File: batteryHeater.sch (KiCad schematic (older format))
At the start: 30 parts

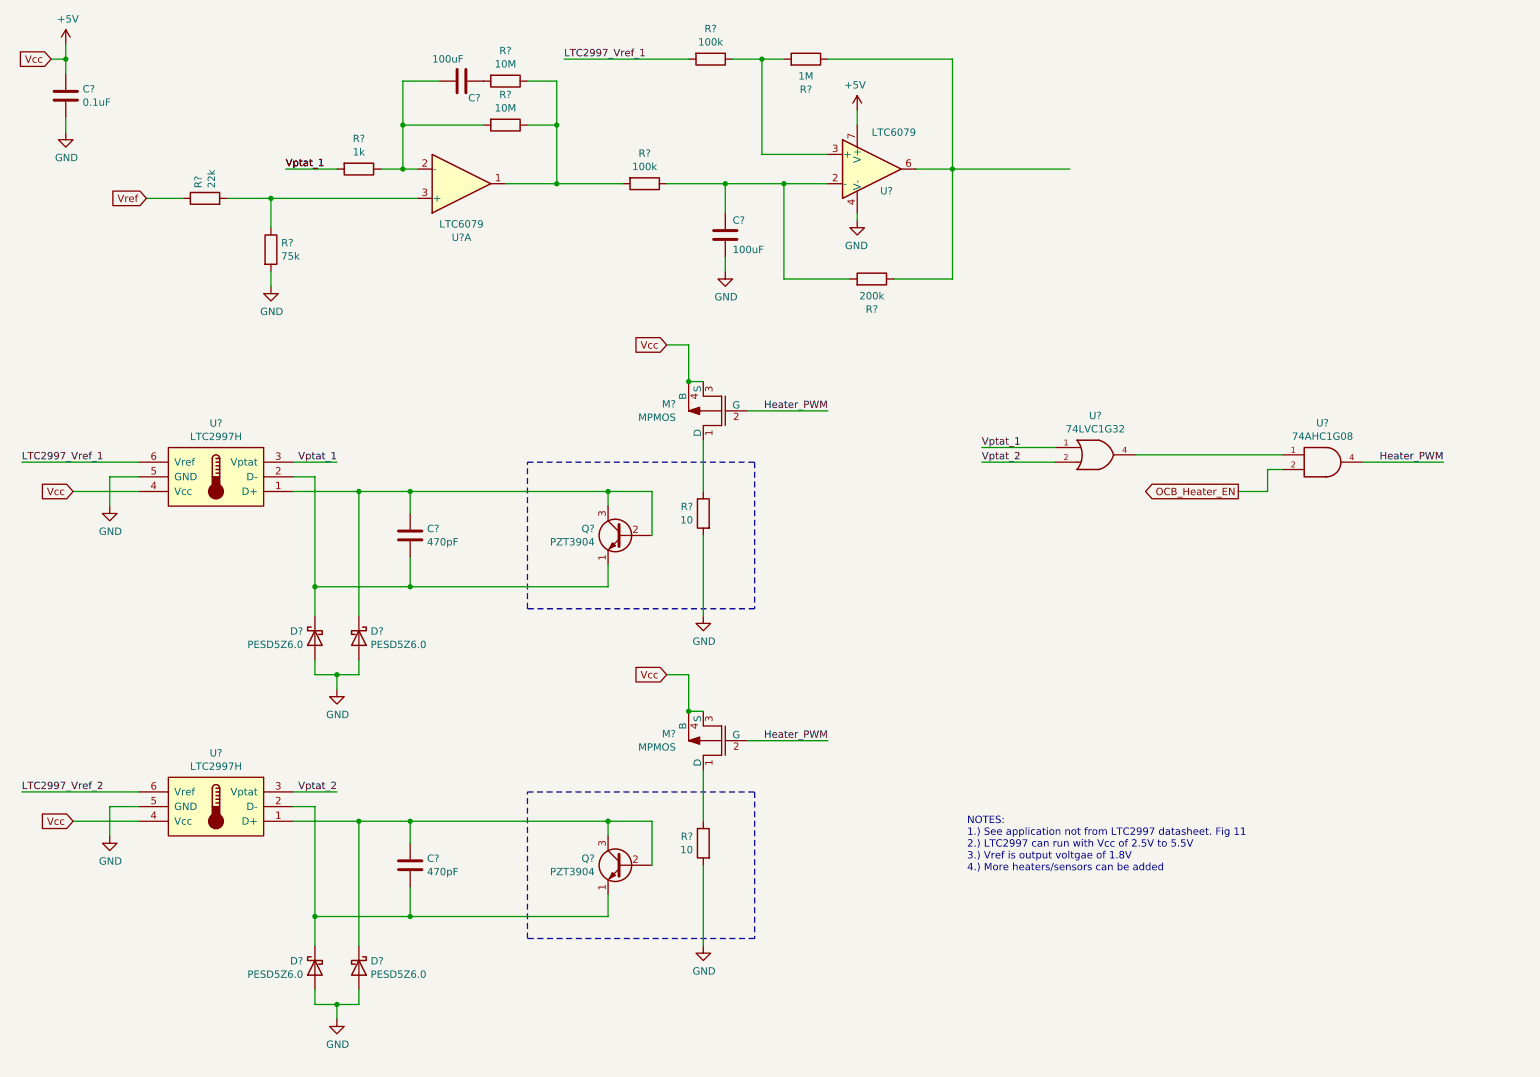
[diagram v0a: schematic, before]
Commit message: added notes for battery heater circuit.
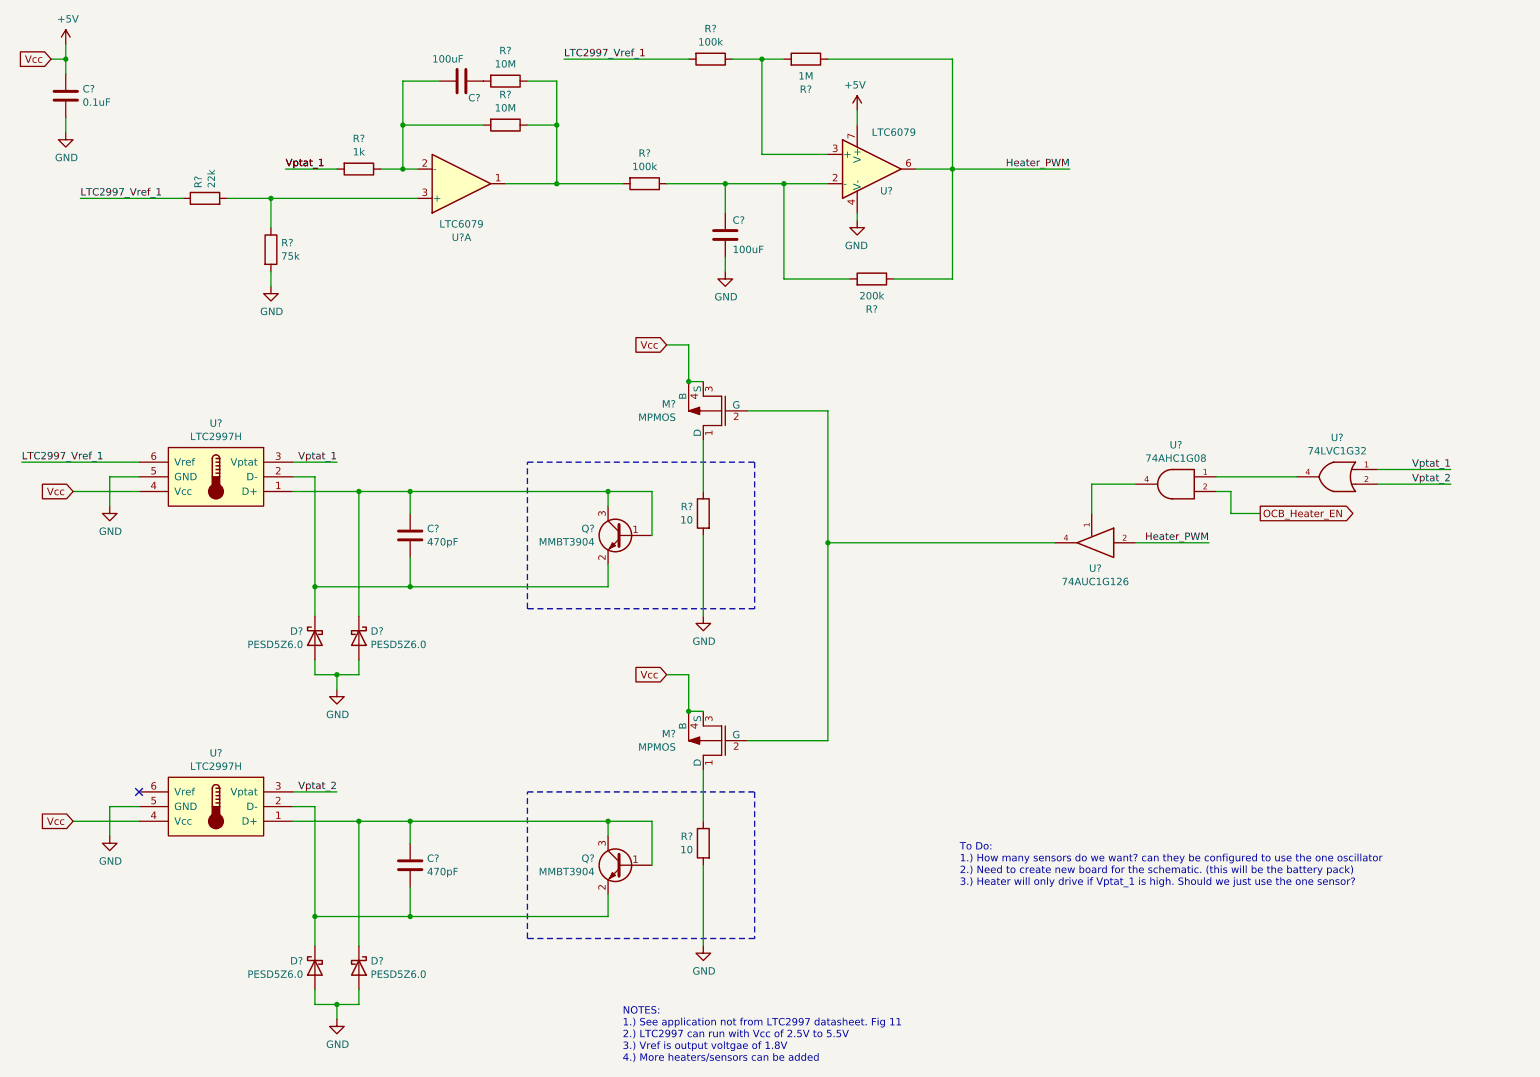
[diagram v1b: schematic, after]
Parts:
- removed Q? (x2): PZT3904, Package_TO_SOT_THT:TO-92_Inline, symbol Main-rescue:2N3904-Transistor_BJT
- added Q? (x2): MMBT3904, Package_TO_SOT_SMD:SOT-23, symbol Transistor_BJT:MMBT3904
- added U?: 74AUC1G126, symbol 74xGxx:74AUC1G126
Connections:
- net Vref is gone; now on net LTC2997_Vref_1: R?.1
- net GND: now also U?.3 (GND)
- net Heater_PWM: now also R?.1, R?.1, U?.6, U?.2; no longer M?.2 (G), M?.2 (G), U?.4
- net VCC: now also U?.5 (VCC)
- net at C?.1, D?.1 (K), U?.1 (D+): now also Q?.1 (B), Q?.3 (C) (x2)
- net at C?.2, D?.1 (K), U?.2 (D-): now also Q?.2 (E) (x2)
- net LTC2997_Vref_2: no longer names the net of U?.6 (Vref)
- new net: M?.2 (G), M?.2 (G), U?.4
- new net: U?.1, U?.4
- no-connect marks 0 -> 1
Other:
- note added: "To Do:\n1.) How many sensors do we want? can they be configured to use the one oscillator\n2.) Need to create new board for the schematic. (this will be the battery pack)\n3.) Heater will only drive if Vptat_1 is high. Should we just use the one sensor?\n"
- moved on the sheet: U?
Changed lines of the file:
@@
 	1    0    0    -1
-$EndComp
-$Comp
-L Main-rescue:2N3904-Transistor_BJT Q?
-U 1 1 5D1F5D3D
-P 4700 4100
-F 0 "Q?" H 4891 4146 50  0000 L CNN
-F 1 "PZT3904" H 4891 4055 50  0000 L CNN
-F 2 "Package_TO_SOT_THT:TO-92_Inline" H 4900 4025 50  0001 L CIN
-F 3 "https://www.fairchildsemi.com/datasheets/2N/2N3904.pdf" H 4700 4100 50  0001 L CNN
-	1    4700 4100
-	-1   0    0    -1
 $EndComp
 Wire Wire Line
@@
 Wire Wire Line
 	6100 1500 5650 1500
-Text GLabel 1450 1800 0    50   Input ~ 0
-Vref
 Wire Wire Line
 	900  750  900  850
@@
 $EndComp
 Wire Wire Line
-	1450 1800 1700 1800
-Wire Wire Line
 	2000 1800 2300 1800
 Connection ~ 2300 1800
@@
 Wire Wire Line
 	6950 1600 7750 1600
-Text Label 10300 3600 2    50   ~ 0
-Heater_PWM
 Wire Wire Line
 	1400 3600 600  3600
@@
 Wire Wire Line
 	6950 2350 6950 1600
-Text Label 6100 3250 2    50   ~ 0
-Heater_PWM
 Wire Wire Line
 	5550 3250 6100 3250
@@
 	1    3250 6350
 	1    0    0    -1
-$EndComp
-$Comp
-L Main-rescue:2N3904-Transistor_BJT Q?
-U 1 1 5E560E1B
-P 4700 6350
-F 0 "Q?" H 4891 6396 50  0000 L CNN
-F 1 "PZT3904" H 4891 6305 50  0000 L CNN
-F 2 "Package_TO_SOT_THT:TO-92_Inline" H 4900 6275 50  0001 L CIN
-F 3 "https://www.fairchildsemi.com/datasheets/2N/2N3904.pdf" H 4700 6350 50  0001 L CNN
-	1    4700 6350
-	-1   0    0    -1
 $EndComp
 Wire Wire Line
@@
 	-1   0    0    -1
 $EndComp
-Wire Wire Line
-	1400 5850 600  5850
-Text Label 600  5850 0    50   ~ 0
-LTC2997_Vref_2
 $Comp
 L Device:D_Schottky D?
@@
 Wire Wire Line
 	2750 7300 2600 7300
-Text Label 6100 5500 2    50   ~ 0
-Heater_PWM
 Wire Wire Line
 	5550 5500 6100 5500
@@
 L 74xGxx:74LVC1G32 U?
 U 1 1 5E56CF68
-P 7950 3550
-F 0 "U?" H 7925 3817 50  0000 C CNN
-F 1 "74LVC1G32" H 7925 3726 50  0000 C CNN
-F 2 "" H 7950 3550 50  0001 C CNN
-F 3 "http://www.ti.com/lit/sg/scyt129e/scyt129e.pdf" H 7950 3550 50  0001 C CNN
-	1    7950 3550
-	1    0    0    -1
+P 9550 3700
+F 0 "U?" H 9525 3967 50  0000 C CNN
+F 1 "74LVC1G32" H 9525 3876 50  0000 C CNN
+F 2 "" H 9550 3700 50  0001 C CNN
+F 3 "http://www.ti.com/lit/sg/scyt129e/scyt129e.pdf" H 9550 3700 50  0001 C CNN
+	1    9550 3700
+	-1   0    0    -1
 $EndComp
 $Comp
 L 74xGxx:74AHC1G08 U?
 U 1 1 5E56DEF1
-P 9500 3600
-F 0 "U?" H 9475 3867 50  0000 C CNN
-F 1 "74AHC1G08" H 9475 3776 50  0000 C CNN
-F 2 "" H 9500 3600 50  0001 C CNN
-F 3 "http://www.ti.com/lit/sg/scyt129e/scyt129e.pdf" H 9500 3600 50  0001 C CNN
-	1    9500 3600
-	1    0    0    -1
-$EndComp
-Wire Wire Line
-	9750 3600 10300 3600
-Text Label 7150 3500 0    50   ~ 0
+P 8450 3750
+F 0 "U?" H 8425 4017 50  0000 C CNN
+F 1 "74AHC1G08" H 8425 3926 50  0000 C CNN
+F 2 "" H 8450 3750 50  0001 C CNN
+F 3 "http://www.ti.com/lit/sg/scyt129e/scyt129e.pdf" H 8450 3750 50  0001 C CNN
+	1    8450 3750
+	-1   0    0    -1
+$EndComp
+Wire Wire Line
+	8200 3750 7900 3750
+Text Label 10350 3650 2    50   ~ 0
 Vptat_1
-Text Label 7150 3600 0    50   ~ 0
+Text Label 10350 3750 2    50   ~ 0
 Vptat_2
 Wire Wire Line
-	7150 3500 7650 3500
-Wire Wire Line
-	7650 3600 7150 3600
-Wire Wire Line
-	9200 3650 9100 3650
-Wire Wire Line
-	9100 3650 9100 3800
-Text GLabel 8900 3800 0    50   Output ~ 0
+	10350 3650 9850 3650
+Wire Wire Line
+	9850 3750 10350 3750
+Wire Wire Line
+	8750 3800 8850 3800
+Wire Wire Line
+	8850 3800 8850 3950
+Text GLabel 9050 3950 2    50   Output ~ 0
 OCB_Heater_EN
 Wire Wire Line
-	8900 3800 9100 3800
-Wire Wire Line
-	8200 3550 9200 3550
-Text Notes 7050 6400 0    50   ~ 0
+	9050 3950 8850 3950
+Text Notes 4700 7700 0    50   ~ 0
 NOTES:\n1.) See application not from LTC2997 datasheet. Fig 11\n2.) LTC2997 can run with Vcc of 2.5V to 5.5V\n3.) Vref is output voltgae of 1.8V\n4.) More heaters/sensors can be added
+Text Label 7750 1600 2    50   ~ 0
+Heater_PWM
+Text Label 1000 1800 0    50   ~ 0
+LTC2997_Vref_1
+Wire Wire Line
+	1000 1800 1700 1800
+NoConn ~ 1400 5850
+$Comp
+L Transistor_BJT:MMBT3904 Q?
+U 1 1 5E3D63BD
+P 4700 6350
+F 0 "Q?" H 4891 6396 50  0000 L CNN
+F 1 "MMBT3904" H 4891 6305 50  0000 L CNN
+F 2 "Package_TO_SOT_SMD:SOT-23" H 4900 6275 50  0001 L CIN
+F 3 "https://www.fairchildsemi.com/datasheets/2N/2N3904.pdf" H 4700 6350 50  0001 L CNN
+	1    4700 6350
+	-1   0    0    -1
+$EndComp
+$Comp
+L Transistor_BJT:MMBT3904 Q?
+U 1 1 5E3E16A3
+P 4700 4100
+F 0 "Q?" H 4891 4146 50  0000 L CNN
+F 1 "MMBT3904" H 4891 4055 50  0000 L CNN
+F 2 "Package_TO_SOT_SMD:SOT-23" H 4900 4025 50  0001 L CIN
+F 3 "https://www.fairchildsemi.com/datasheets/2N/2N3904.pdf" H 4700 4100 50  0001 L CNN
+	1    4700 4100
+	-1   0    0    -1
+$EndComp
+Text Notes 7000 6500 0    50   ~ 0
+To Do:\n1.) How many sensors do we want? can they be configured to use the one oscillator\n2.) Need to create new board for the schematic. (this will be the battery pack)\n3.) Heater will only drive if Vptat_1 is high. Should we just use the one sensor?\n
+Wire Wire Line
+	9300 3700 8750 3700
+$Comp
+L 74xGxx:74AUC1G126 U?
+U 1 1 5E3EB5FA
+P 7900 4150
+F 0 "U?" H 7875 3975 50  0000 C CNN
+F 1 "74AUC1G126" H 7875 3884 50  0000 C CNN
+F 2 "" H 7900 4150 50  0001 C CNN
+F 3 "http://www.ti.com/lit/sg/scyt129e/scyt129e.pdf" H 7900 4150 50  0001 C CNN
+	1    7900 4150
+	-1   0    0    -1
+$EndComp
+Wire Wire Line
+	7900 3950 7900 3750
+Text Label 8700 4150 2    50   ~ 0
+Heater_PWM
+Wire Wire Line
+	8200 4150 8700 4150
+Wire Wire Line
+	6100 4150 7650 4150
+Connection ~ 6100 4150
+Wire Wire Line
+	6100 4150 6100 5500
+Wire Wire Line
+	6100 3250 6100 4150
 $EndSCHEMATC

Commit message: Fixed heater circuit to trigger at 0C. Removed TVS diodes
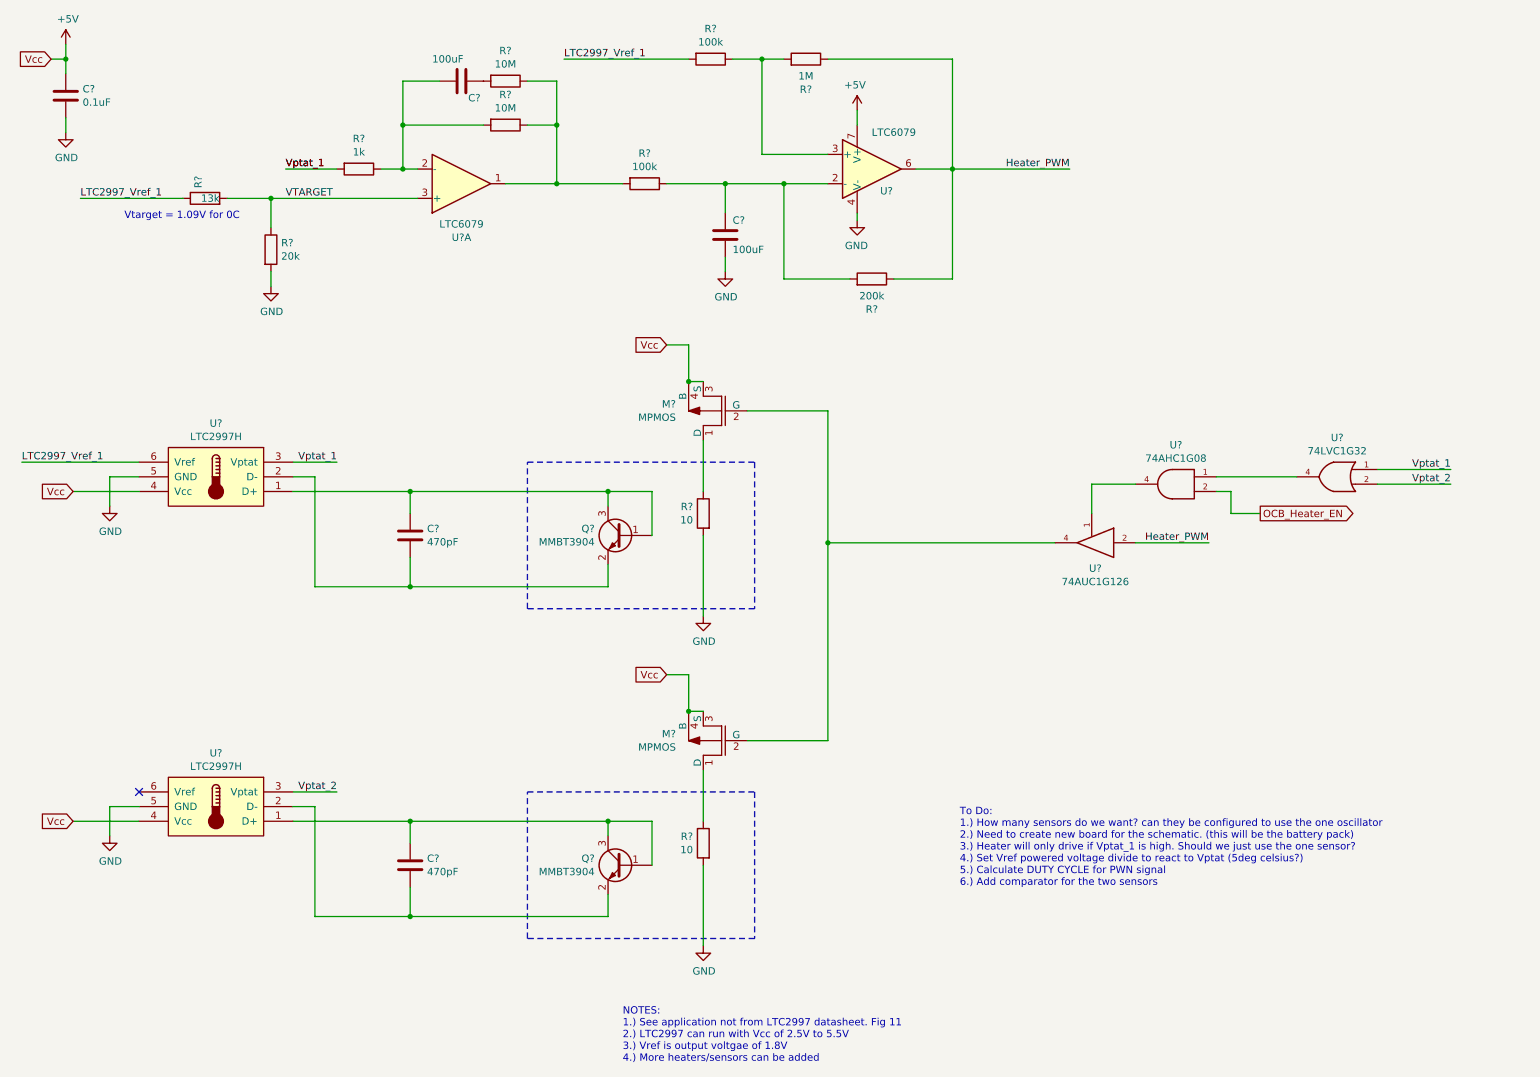
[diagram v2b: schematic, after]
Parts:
- removed D? (x4): PESD5Z6.0, symbol Device:D_Schottky
- R?: value 22k -> 13k
- R?: value 75k -> 20k
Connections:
- net VTARGET: now reaches R?.1, R?.2, U?.3 (+)
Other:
- note added: "To Do:\n1.) How many sensors do we want? can they be configured to use the one oscillator\n2.) Need to create new board for the schematic. (this will be the battery pack)\n3.) Heater will only drive if Vptat_1 is high. Should we just use the one sensor?\n4.) Set Vref powered voltage divide to react to Vptat (5deg celsius?)\n5.) Calculate DUTY CYCLE for PWN signal\n6.) Add comparator for the two s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"
- note added: "Vtarget = 1.09V for 0C"
- note removed: "To Do:\n1.) How many sensors do we want? can they be configured to use the one oscillator\n2.) Need to create new board for the schematic. (this will be the battery pack)\n3.) Heater will only drive if Vptat_1 is high. Should we just use the one sensor?\n"
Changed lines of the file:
@@
 Wire Wire Line
 	3250 3800 3250 3950
-Wire Wire Line
-	2450 3800 2900 3800
 $Comp
 L Main-rescue:C-Device C?
@@
 P 1850 1800
 F 0 "R?" H 1920 1846 50  0000 L CNN
-F 1 "22k" H 1920 1755 50  0000 L CNN
+F 1 "13k" V 1850 1700 50  0000 L CNN
 F 2 "Resistors_SMD:R_0805_HandSoldering" V 1780 1800 50  0001 C CNN
 F 3 "~" H 1850 1800 50  0001 C CNN
@@
 P 2300 2150
 F 0 "R?" H 2370 2196 50  0000 L CNN
-F 1 "75k" H 2370 2105 50  0000 L CNN
+F 1 "20k" H 2370 2105 50  0000 L CNN
 F 2 "Resistors_SMD:R_0805_HandSoldering" V 2230 2150 50  0001 C CNN
 F 3 "~" H 2300 2150 50  0001 C CNN
@@
 Text Label 600  3600 0    50   ~ 0
 LTC2997_Vref_1
-$Comp
-L Device:D_Schottky D?
-U 1 1 5E4D9DA5
-P 2900 4800
-F 0 "D?" V 2854 4880 50  0000 L CNN
-F 1 "PESD5Z6.0" V 2945 4880 50  0000 L CNN
-F 2 "" H 2900 4800 50  0001 C CNN
-F 3 "" H 2900 4800 50  0001 C CNN
-	1    2900 4800
-	0    1    1    0
-$EndComp
-$Comp
-L Device:D_Schottky D?
-U 1 1 5E4DAD1B
-P 2600 4800
-F 0 "D?" V 2554 4880 50  0000 L CNN
-F 1 "PESD5Z6.0" V 2645 4880 50  0000 L CNN
-F 2 "" H 2600 4800 50  0001 C CNN
-F 3 "" H 2600 4800 50  0001 C CNN
-	1    2600 4800
-	0    -1   1    0
-$EndComp
 Wire Wire Line
 	2600 3700 2450 3700
@@
 	3250 4450 2600 4450
 Connection ~ 3250 4450
-Connection ~ 2600 4450
-Wire Wire Line
-	2600 4450 2600 4650
-Wire Wire Line
-	2900 4650 2900 3800
-Connection ~ 2900 3800
-Wire Wire Line
-	2900 3800 3250 3800
-Wire Wire Line
-	2900 4950 2900 5050
-Wire Wire Line
-	2900 5050 2750 5050
-Wire Wire Line
-	2600 5050 2600 4950
-$Comp
-L Main-rescue:GND-power #PWR?
-U 1 1 5E4EB388
-P 2750 5150
-F 0 "#PWR?" H 2750 4900 50  0001 C CNN
-F 1 "GND" H 2755 4977 50  0000 C CNN
-F 2 "" H 2750 5150 50  0001 C CNN
-F 3 "" H 2750 5150 50  0001 C CNN
-	1    2750 5150
-	1    0    0    -1
-$EndComp
-Wire Wire Line
-	2750 5150 2750 5050
-Connection ~ 2750 5050
-Wire Wire Line
-	2750 5050 2600 5050
 $Comp
 L Main-rescue:R-Device R?
@@
 Wire Wire Line
 	3250 6050 3250 6200
-Wire Wire Line
-	2450 6050 2900 6050
 $Comp
 L Main-rescue:C-Device C?
@@
 	-1   0    0    -1
 $EndComp
-$Comp
-L Device:D_Schottky D?
-U 1 1 5E560E4A
-P 2900 7050
-F 0 "D?" V 2854 7130 50  0000 L CNN
-F 1 "PESD5Z6.0" V 2945 7130 50  0000 L CNN
-F 2 "" H 2900 7050 50  0001 C CNN
-F 3 "" H 2900 7050 50  0001 C CNN
-	1    2900 7050
-	0    1    1    0
-$EndComp
-$Comp
-L Device:D_Schottky D?
-U 1 1 5E560E50
-P 2600 7050
-F 0 "D?" V 2554 7130 50  0000 L CNN
-F 1 "PESD5Z6.0" V 2645 7130 50  0000 L CNN
-F 2 "" H 2600 7050 50  0001 C CNN
-F 3 "" H 2600 7050 50  0001 C CNN
-	1    2600 7050
-	0    -1   1    0
-$EndComp
 Wire Wire Line
 	2600 5950 2450 5950
@@
 	3250 6700 2600 6700
 Connection ~ 3250 6700
-Connection ~ 2600 6700
-Wire Wire Line
-	2600 6700 2600 6900
-Wire Wire Line
-	2900 6900 2900 6050
-Connection ~ 2900 6050
-Wire Wire Line
-	2900 6050 3250 6050
-Wire Wire Line
-	2900 7200 2900 7300
-Wire Wire Line
-	2900 7300 2750 7300
-Wire Wire Line
-	2600 7300 2600 7200
-$Comp
-L Main-rescue:GND-power #PWR?
-U 1 1 5E560E62
-P 2750 7400
-F 0 "#PWR?" H 2750 7150 50  0001 C CNN
-F 1 "GND" H 2755 7227 50  0000 C CNN
-F 2 "" H 2750 7400 50  0001 C CNN
-F 3 "" H 2750 7400 50  0001 C CNN
-	1    2750 7400
-	1    0    0    -1
-$EndComp
-Wire Wire Line
-	2750 7400 2750 7300
-Connection ~ 2750 7300
-Wire Wire Line
-	2750 7300 2600 7300
 Wire Wire Line
 	5550 5500 6100 5500
@@
 $EndComp
 Text Notes 7000 6500 0    50   ~ 0
-To Do:\n1.) How many sensors do we want? can they be configured to use the one oscillator\n2.) Need to create new board for the schematic. (this will be the battery pack)\n3.) Heater will only drive if Vptat_1 is high. Should we just use the one sensor?\n
+To Do:\n1.) How many sensors do we want? can they be configured to use the one oscillator\n2.) Need to create new board for the schematic. (this will be the battery pack)\n3.) Heater will only drive if Vptat_1 is high. Should we just use the one sensor?\n4.) Set Vref powered voltage divide to react to Vptat (5deg celsius?)\n5.) Calculate DUTY CYCLE for PWN signal\n6.) Add comparator for the two sensors
 Wire Wire Line
 	9300 3700 8750 3700
@@
 Wire Wire Line
 	6100 3250 6100 4150
+Text Notes 1300 1950 0    50   ~ 0
+Vtarget = 1.09V for 0C
+Text Label 2400 1800 0    50   ~ 0
+VTARGET
+Wire Wire Line
+	2450 3800 3250 3800
+Wire Wire Line
+	2450 6050 3250 6050
 $EndSCHEMATC
